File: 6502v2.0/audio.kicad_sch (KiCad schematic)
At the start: 22 parts, among them J16 AudioPlug3, U13 PSG_AY-3-8910, U15 PSG_AY-3-8910

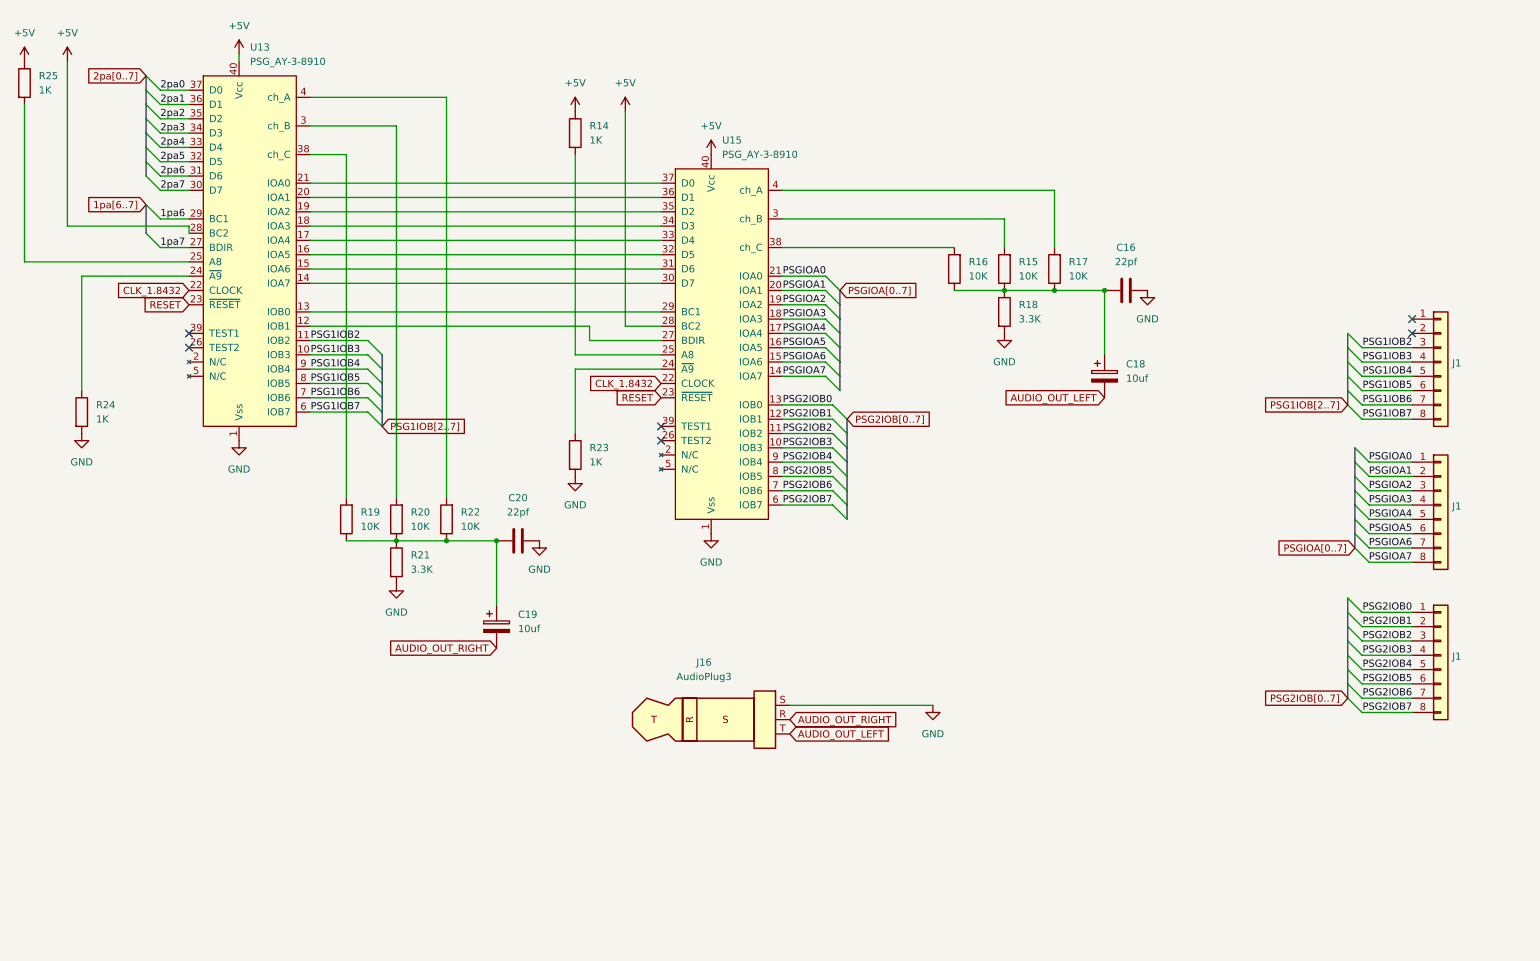
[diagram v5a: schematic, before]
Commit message: moved video to seperate folder, cleaned schematic
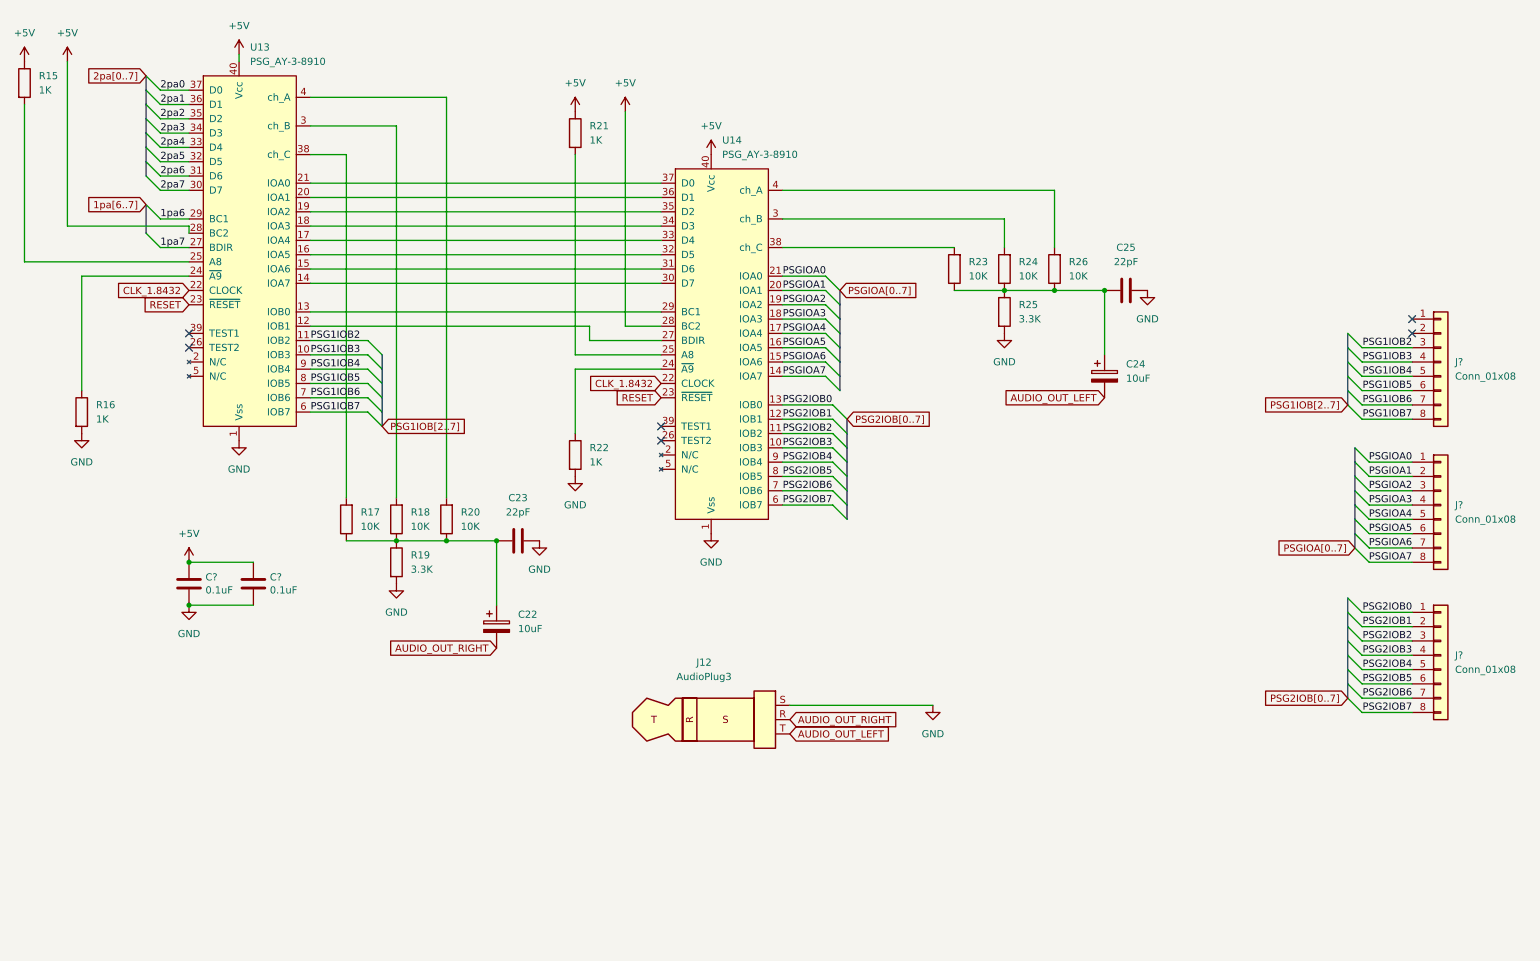
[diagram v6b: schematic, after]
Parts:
- removed J1 (x3): ~, symbol Connector_Generic:Conn_01x08
- added C? (x2): 0.1uF, Capacitor_THT:C_Disc_D5.1mm_W3.2mm_P5.00mm, symbol Device:C
- added J? (x3): Conn_01x08, Connector_PinHeader_2.54mm:PinHeader_1x08_P2.54mm_Vertical, symbol Connector_Generic:Conn_01x08
- C22: renamed from C19; value 10uf -> 10uF
- C23: renamed from C20; value 22pf -> 22pF
- C24: renamed from C18; value 10uf -> 10uF
- C25: renamed from C16; value 22pf -> 22pF
- J12: renamed from J16; footprint (none) -> 8bits:AUDIO-JACK
- R15: renamed from R25; footprint Resistor_THT:R_Axial_DIN0204_L3.6mm_D1.6mm_P7.62mm_Horizontal -> Resistor_THT:R_Axial_DIN0207_L6.3mm_D2.5mm_P10.16mm_Horizontal
- R16: renamed from R24; footprint Resistor_THT:R_Axial_DIN0204_L3.6mm_D1.6mm_P7.62mm_Horizontal -> Resistor_THT:R_Axial_DIN0207_L6.3mm_D2.5mm_P10.16mm_Horizontal
- R17: renamed from R19; footprint Resistor_THT:R_Axial_DIN0204_L3.6mm_D1.6mm_P7.62mm_Horizontal -> Resistor_THT:R_Axial_DIN0207_L6.3mm_D2.5mm_P10.16mm_Horizontal
- R18: renamed from R20; footprint Resistor_THT:R_Axial_DIN0204_L3.6mm_D1.6mm_P7.62mm_Horizontal -> Resistor_THT:R_Axial_DIN0207_L6.3mm_D2.5mm_P10.16mm_Horizontal
- R19: renamed from R21; footprint Resistor_THT:R_Axial_DIN0204_L3.6mm_D1.6mm_P7.62mm_Horizontal -> Resistor_THT:R_Axial_DIN0207_L6.3mm_D2.5mm_P10.16mm_Horizontal
- R20: renamed from R22; footprint Resistor_THT:R_Axial_DIN0204_L3.6mm_D1.6mm_P7.62mm_Horizontal -> Resistor_THT:R_Axial_DIN0207_L6.3mm_D2.5mm_P10.16mm_Horizontal
- R21: renamed from R14; footprint Resistor_THT:R_Axial_DIN0204_L3.6mm_D1.6mm_P7.62mm_Horizontal -> Resistor_THT:R_Axial_DIN0207_L6.3mm_D2.5mm_P10.16mm_Horizontal
- R22: renamed from R23; footprint Resistor_THT:R_Axial_DIN0204_L3.6mm_D1.6mm_P7.62mm_Horizontal -> Resistor_THT:R_Axial_DIN0207_L6.3mm_D2.5mm_P10.16mm_Horizontal
- R23: renamed from R16; footprint Resistor_THT:R_Axial_DIN0204_L3.6mm_D1.6mm_P7.62mm_Horizontal -> Resistor_THT:R_Axial_DIN0207_L6.3mm_D2.5mm_P10.16mm_Horizontal
- R24: renamed from R15; footprint Resistor_THT:R_Axial_DIN0204_L3.6mm_D1.6mm_P7.62mm_Horizontal -> Resistor_THT:R_Axial_DIN0207_L6.3mm_D2.5mm_P10.16mm_Horizontal
- R25: renamed from R18; footprint Resistor_THT:R_Axial_DIN0204_L3.6mm_D1.6mm_P7.62mm_Horizontal -> Resistor_THT:R_Axial_DIN0207_L6.3mm_D2.5mm_P10.16mm_Horizontal
- R26: renamed from R17; footprint Resistor_THT:R_Axial_DIN0204_L3.6mm_D1.6mm_P7.62mm_Horizontal -> Resistor_THT:R_Axial_DIN0207_L6.3mm_D2.5mm_P10.16mm_Horizontal
- renumbered U15 to U14
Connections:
- net +5V: now also C?.1, C?.1
- net GND: now also C?.2, C?.2
- net PSG1IOB2: now also J?.3 (Pin_3)
- net PSG1IOB3: now also J?.4 (Pin_4)
- net PSG1IOB4: now also J?.5 (Pin_5)
- net PSG1IOB5: now also J?.6 (Pin_6)
- net PSG1IOB6: now also J?.7 (Pin_7)
- net PSG1IOB7: now also J?.8 (Pin_8)
- net PSG2IOB0: now also J?.1 (Pin_1)
- net PSG2IOB1: now also J?.2 (Pin_2)
- net PSG2IOB2: now also J?.3 (Pin_3)
- net PSG2IOB3: now also J?.4 (Pin_4)
- net PSG2IOB4: now also J?.5 (Pin_5)
- net PSG2IOB5: now also J?.6 (Pin_6)
- net PSG2IOB6: now also J?.7 (Pin_7)
- net PSG2IOB7: now also J?.8 (Pin_8)
- net PSGIOA0: now also J?.1 (Pin_1)
- net PSGIOA1: now also J?.2 (Pin_2)
- net PSGIOA2: now also J?.3 (Pin_3)
- net PSGIOA3: now also J?.4 (Pin_4)
- net PSGIOA4: now also J?.5 (Pin_5)
- net PSGIOA5: now also J?.6 (Pin_6)
- net PSGIOA6: now also J?.7 (Pin_7)
- net PSGIOA7: now also J?.8 (Pin_8)

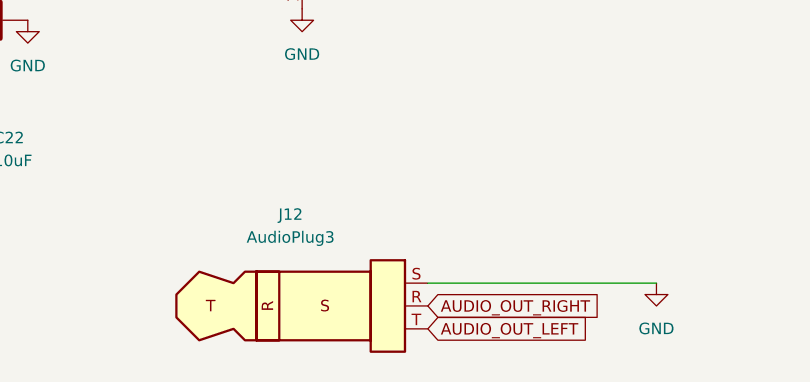
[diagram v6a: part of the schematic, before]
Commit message: rearranged directory structure.
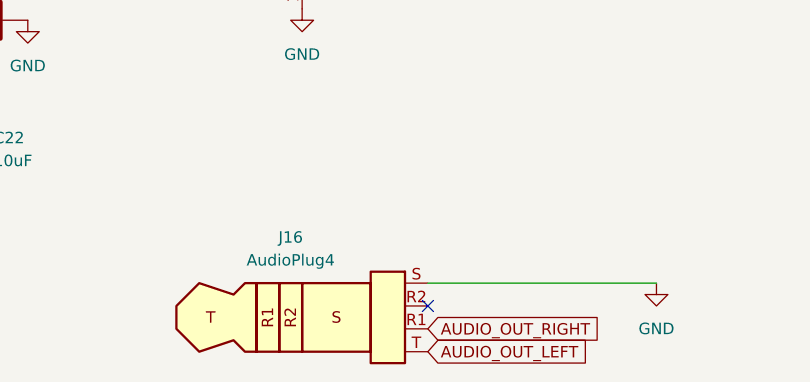
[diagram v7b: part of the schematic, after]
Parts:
- removed J12: AudioPlug3, 8bits:AUDIO-JACK, symbol Connector_Audio:AudioPlug3
- added J16: AudioPlug4, symbol Connector_Audio:AudioPlug4
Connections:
- net AUDIO_OUT_LEFT: now also J16.T
- net AUDIO_OUT_RIGHT: now also J16.R1
- net GND: now also J16.S
- no-connect marks 6 -> 7
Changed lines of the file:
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@@
   (no_connect (at 264.16 81.28))
   (no_connect (at 46.99 83.82))
+  (no_connect (at 153.67 149.86))
   (no_connect (at 130.81 97.79))
   (no_connect (at 46.99 81.28))
@@
     (effects (font (size 1.27 1.27)) (justify right bottom))
   )
-  (global_label "AUDIO_OUT_LEFT" (shape input) (at 153.67 152.4 0) (fields_autoplaced)
+  (global_label "AUDIO_OUT_LEFT" (shape input) (at 153.67 154.94 0) (fields_autoplaced)
     (effects (font (size 1.27 1.27)) (justify left))
-    (property "Intersheetrefs" "${INTERSHEET_REFS}" (at 171.9973 152.4 0)
+    (property "Intersheetrefs" "${INTERSHEET_REFS}" (at 171.9973 154.94 0)
       (effects (font (size 1.27 1.27)) (justify left) hide)
     )
@@
     )
   )
-  (global_label "AUDIO_OUT_RIGHT" (shape input) (at 153.67 149.86 0) (fields_autoplaced)
+  (global_label "AUDIO_OUT_RIGHT" (shape input) (at 153.67 152.4 0) (fields_autoplaced)
     (effects (font (size 1.27 1.27)) (justify left))
-    (property "Intersheetrefs" "${INTERSHEET_REFS}" (at 173.2069 149.86 0)
+    (property "Intersheetrefs" "${INTERSHEET_REFS}" (at 173.2069 152.4 0)
       (effects (font (size 1.27 1.27)) (justify left) hide)
     )
@@
     )
   )
-  (symbol (lib_id "Connector_Audio:AudioPlug3") (at 138.43 149.86 0) (unit 1)
-    (in_bom yes) (on_board yes) (dnp no) (fields_autoplaced)
-    (property "Reference" "J12" (at 138.43 139.7 0)
-      (effects (font (size 1.27 1.27)))
-    )
-    (property "Value" "AudioPlug3" (at 138.43 142.24 0)
-      (effects (font (size 1.27 1.27)))
-    )
-    (property "Footprint" "8bits:AUDIO-JACK" (at 140.97 151.13 0)
-      (effects (font (size 1.27 1.27)) hide)
-    )
-    (property "Datasheet" "~" (at 140.97 151.13 0)
-      (effects (font (size 1.27 1.27)) hide)
-    )
-    (pin "R")
-    (pin "S")
-    (pin "T")
-    (instances
-      (project "6502v2.0"
-        (path "/5ffbcd12-d35a-40f1-aa31-5cc41b65e9d8/99446e73-4cf8-4cf8-b0e5-2db38fecee4d"
-          (reference "J12") (unit 1)
-        )
-      )
-    )
-  )
   (symbol (lib_id "Device:C_Polarized") (at 209.55 88.9 0) (unit 1)
     (in_bom yes) (on_board yes) (dnp no) (fields_autoplaced)
@@
         )
       )
+    )
+  )
+  (symbol (lib_id "Connector_Audio:AudioPlug4") (at 138.43 149.86 0) (unit 1)
+    (in_bom yes) (on_board yes) (dnp no) (fields_autoplaced)
+    (property "Reference" "J16" (at 138.43 142.24 0)
+      (effects (font (size 1.27 1.27)))
+    )
+    (property "Value" "AudioPlug4" (at 138.43 144.78 0)
+      (effects (font (size 1.27 1.27)))
+    )
+    (property "Footprint" "" (at 147.32 152.4 0)
+      (effects (font (size 1.27 1.27)) hide)
+    )
+    (property "Datasheet" "~" (at 147.32 152.4 0)
+      (effects (font (size 1.27 1.27)) hide)
+    )
+    (pin "R1")
+    (pin "R2")
+    (pin "S")
+    (pin "T")
+    (instances
+      (project "6502v2.0"
+        (path "/5ffbcd12-d35a-40f1-aa31-5cc41b65e9d8/99446e73-4cf8-4cf8-b0e5-2db38fecee4d"
+          (reference "J16") (unit 1)
+        )
+      )
